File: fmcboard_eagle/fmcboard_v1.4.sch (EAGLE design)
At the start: 138 parts, among them IC1 OPA699ID, IC10 LTC6229IMS8E#TRPBF, IC11 7805TV, IC12 SN74AUC2G66DCTR, IC13 SN74AUC2G66DCTR, IC14 SN74AUC2G66DCTR, IC15 SN74AUC2G66DCTR, IC16 DAC7578SPWR, IC2 DAC7578SPWR, IC3 LTC6229IMS8E#TRPBF, IC4 LTC6229IMS8E#TRPBF, IC5 LM358, IC6 OPA699ID, IC7 OPA699ID, IC8 LTC6229IMS8E#TRPBF, IC9 LTC6229IMS8E#TRPBF, J1 8pin, J10 8pin, J12 4p-2.54, J2 ASP-134604-01, J3 4p-2.54, J4 4p-2.54, J5 8pin, J6 4p-2.54, J7 4p-2.54, J8 4p-2.54, J9 8pin, U1 TXS0108EPWR, U2 STMICROELECTRONICS_L7905ACVST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

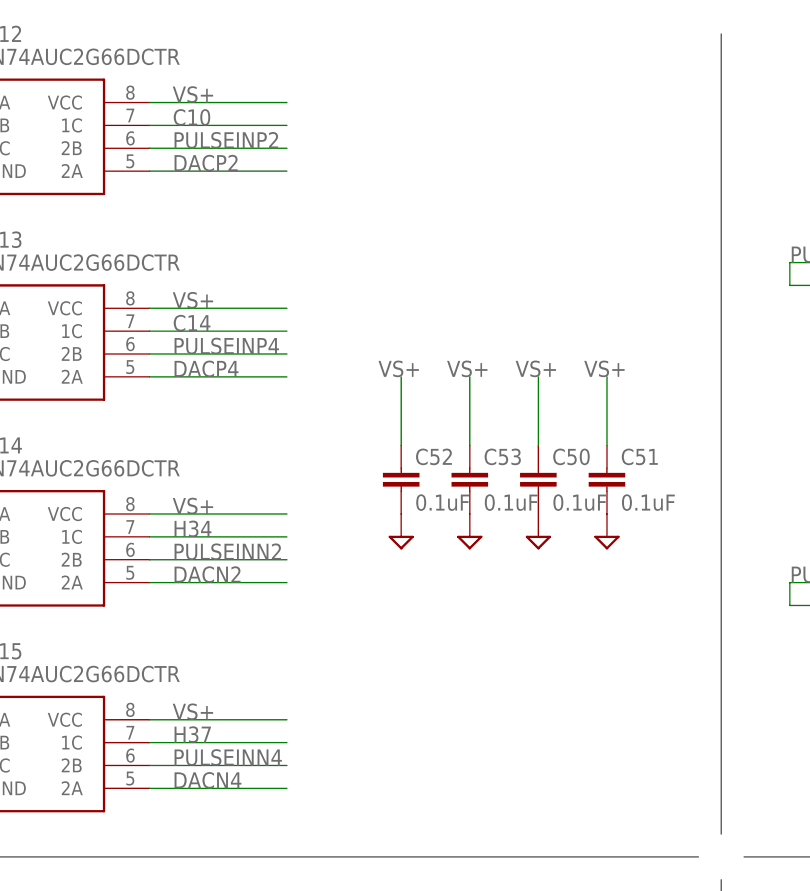
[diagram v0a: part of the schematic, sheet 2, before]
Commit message: v1.41 fix VS+ -> 1V8 for switches
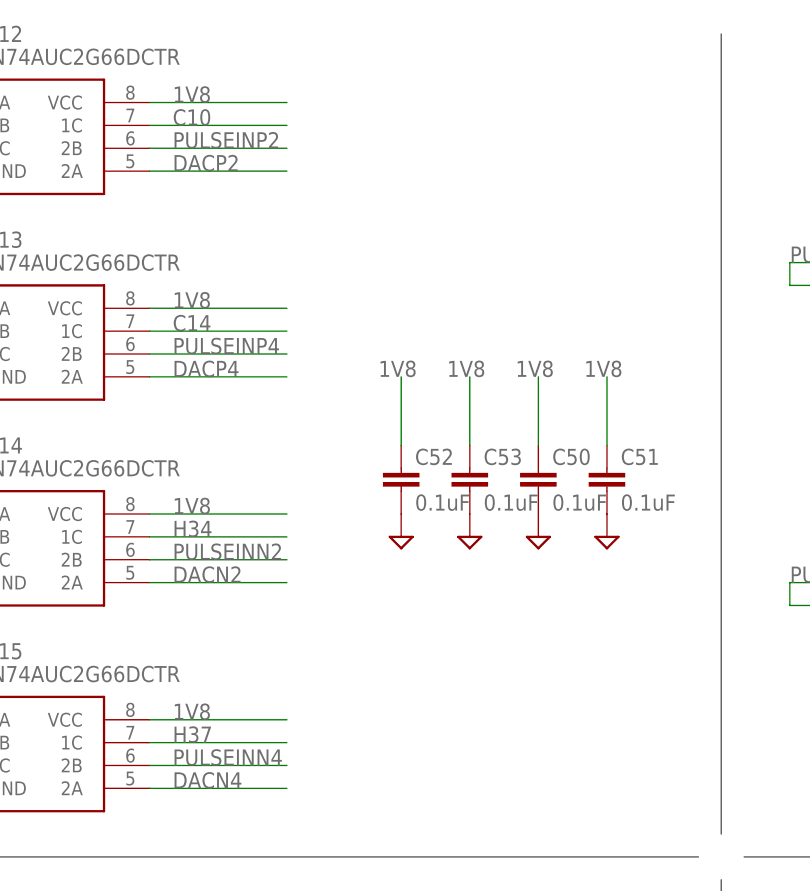
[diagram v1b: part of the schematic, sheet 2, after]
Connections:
- net 1V8: now also C50.1, C51.1, C52.1, C53.1, IC12.VCC, IC13.VCC, IC14.VCC, IC15.VCC
- net VS+: no longer C50.1, C51.1, C52.1, C53.1, IC12.VCC, IC13.VCC, IC14.VCC, IC15.VCC
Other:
- note added: "Pulse and offset DACs"
- note removed: "Pulse DACs"
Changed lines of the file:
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@@
 <text x="132.08" y="114.3" size="1.778" layer="90">Positive output buffers</text>
 <wire x1="190.5" y1="30.48" x2="190.5" y2="119.38" width="0.1524" layer="97"/>
-<text x="81.28" y="114.3" size="1.778" layer="90">Pulse switches</text>
+<text x="86.36" y="114.3" size="1.778" layer="90">Pulse switches</text>
 <wire x1="116.84" y1="27.94" x2="15.24" y2="27.94" width="0.1524" layer="97"/>
 <wire x1="119.38" y1="-15.24" x2="119.38" y2="25.4" width="0.1524" layer="97"/>
 <text x="17.78" y="22.86" size="1.778" layer="90">Pulse resistors for summing</text>
 <wire x1="309.88" y1="27.94" x2="121.92" y2="27.94" width="0.1524" layer="97"/>
-<text x="132.08" y="20.32" size="1.778" layer="90">Pulse DACs</text>
+<text x="132.08" y="20.32" size="1.778" layer="90">Pulse and offset DACs</text>
 </plain>
 <instances>
@@
 <wire x1="259.08" y1="0" x2="259.08" y2="7.62" width="0.1524" layer="91"/>
 <label x="259.08" y="7.62" size="1.778" layer="95"/>
-</segment>
-<segment>
-<pinref part="C52" gate="G$1" pin="1"/>
-<wire x1="83.82" y1="73.66" x2="83.82" y2="81.28" width="0.1524" layer="91"/>
-<label x="81.28" y="81.28" size="1.778" layer="95"/>
-</segment>
-<segment>
-<pinref part="C53" gate="G$1" pin="1"/>
-<wire x1="91.44" y1="73.66" x2="91.44" y2="81.28" width="0.1524" layer="91"/>
-<label x="88.9" y="81.28" size="1.778" layer="95"/>
-</segment>
-<segment>
-<pinref part="C50" gate="G$1" pin="1"/>
-<wire x1="99.06" y1="73.66" x2="99.06" y2="81.28" width="0.1524" layer="91"/>
-<label x="96.52" y="81.28" size="1.778" layer="95"/>
-</segment>
-<segment>
-<pinref part="C51" gate="G$1" pin="1"/>
-<wire x1="106.68" y1="73.66" x2="106.68" y2="81.28" width="0.1524" layer="91"/>
-<label x="104.14" y="81.28" size="1.778" layer="95"/>
-</segment>
-<segment>
-<pinref part="IC12" gate="G$1" pin="VCC"/>
-<wire x1="55.88" y1="111.76" x2="71.12" y2="111.76" width="0.1524" layer="91"/>
-<label x="58.42" y="111.76" size="1.778" layer="95"/>
-</segment>
-<segment>
-<pinref part="IC13" gate="G$1" pin="VCC"/>
-<wire x1="55.88" y1="88.9" x2="71.12" y2="88.9" width="0.1524" layer="91"/>
-<label x="58.42" y="88.9" size="1.778" layer="95"/>
-</segment>
-<segment>
-<pinref part="IC14" gate="G$1" pin="VCC"/>
-<wire x1="55.88" y1="66.04" x2="71.12" y2="66.04" width="0.1524" layer="91"/>
-<label x="58.42" y="66.04" size="1.778" layer="95"/>
-</segment>
-<segment>
-<pinref part="IC15" gate="G$1" pin="VCC"/>
-<wire x1="55.88" y1="43.18" x2="71.12" y2="43.18" width="0.1524" layer="91"/>
-<label x="58.42" y="43.18" size="1.778" layer="95"/>
 </segment>
 <segment>
@@
 <label x="266.7" y="-20.32" size="1.778" layer="95"/>
 </segment>
-</net>
+<segment>
+<pinref part="C52" gate="G$1" pin="1"/>
+<wire x1="83.82" y1="73.66" x2="83.82" y2="81.28" width="0.1524" layer="91"/>
+<label x="81.28" y="81.28" size="1.778" layer="95"/>
+</segment>
+<segment>
+<pinref part="C53" gate="G$1" pin="1"/>
+<wire x1="91.44" y1="73.66" x2="91.44" y2="81.28" width="0.1524" layer="91"/>
+<label x="88.9" y="81.28" size="1.778" layer="95"/>
+</segment>
+<segment>
+<pinref part="C50" gate="G$1" pin="1"/>
+<wire x1="99.06" y1="73.66" x2="99.06" y2="81.28" width="0.1524" layer="91"/>
+<label x="96.52" y="81.28" size="1.778" layer="95"/>
+</segment>
+<segment>
+<pinref part="C51" gate="G$1" pin="1"/>
+<wire x1="106.68" y1="73.66" x2="106.68" y2="81.28" width="0.1524" layer="91"/>
+<label x="104.14" y="81.28" size="1.778" layer="95"/>
+</segment>
+<segment>
+<pinref part="IC12" gate="G$1" pin="VCC"/>
+<wire x1="55.88" y1="111.76" x2="71.12" y2="111.76" width="0.1524" layer="91"/>
+<label x="58.42" y="111.76" size="1.778" layer="95"/>
+</segment>
+<segment>
+<pinref part="IC13" gate="G$1" pin="VCC"/>
+<wire x1="55.88" y1="88.9" x2="71.12" y2="88.9" width="0.1524" layer="91"/>
+<label x="58.42" y="88.9" size="1.778" layer="95"/>
+</segment>
+<segment>
+<pinref part="IC14" gate="G$1" pin="VCC"/>
+<wire x1="55.88" y1="66.04" x2="71.12" y2="66.04" width="0.1524" layer="91"/>
+<label x="58.42" y="66.04" size="1.778" layer="95"/>
+</segment>
+<segment>
+<pinref part="IC15" gate="G$1" pin="VCC"/>
+<wire x1="55.88" y1="43.18" x2="71.12" y2="43.18" width="0.1524" layer="91"/>
+<label x="58.42" y="43.18" size="1.778" layer="95"/>
+</segment>
+</net>

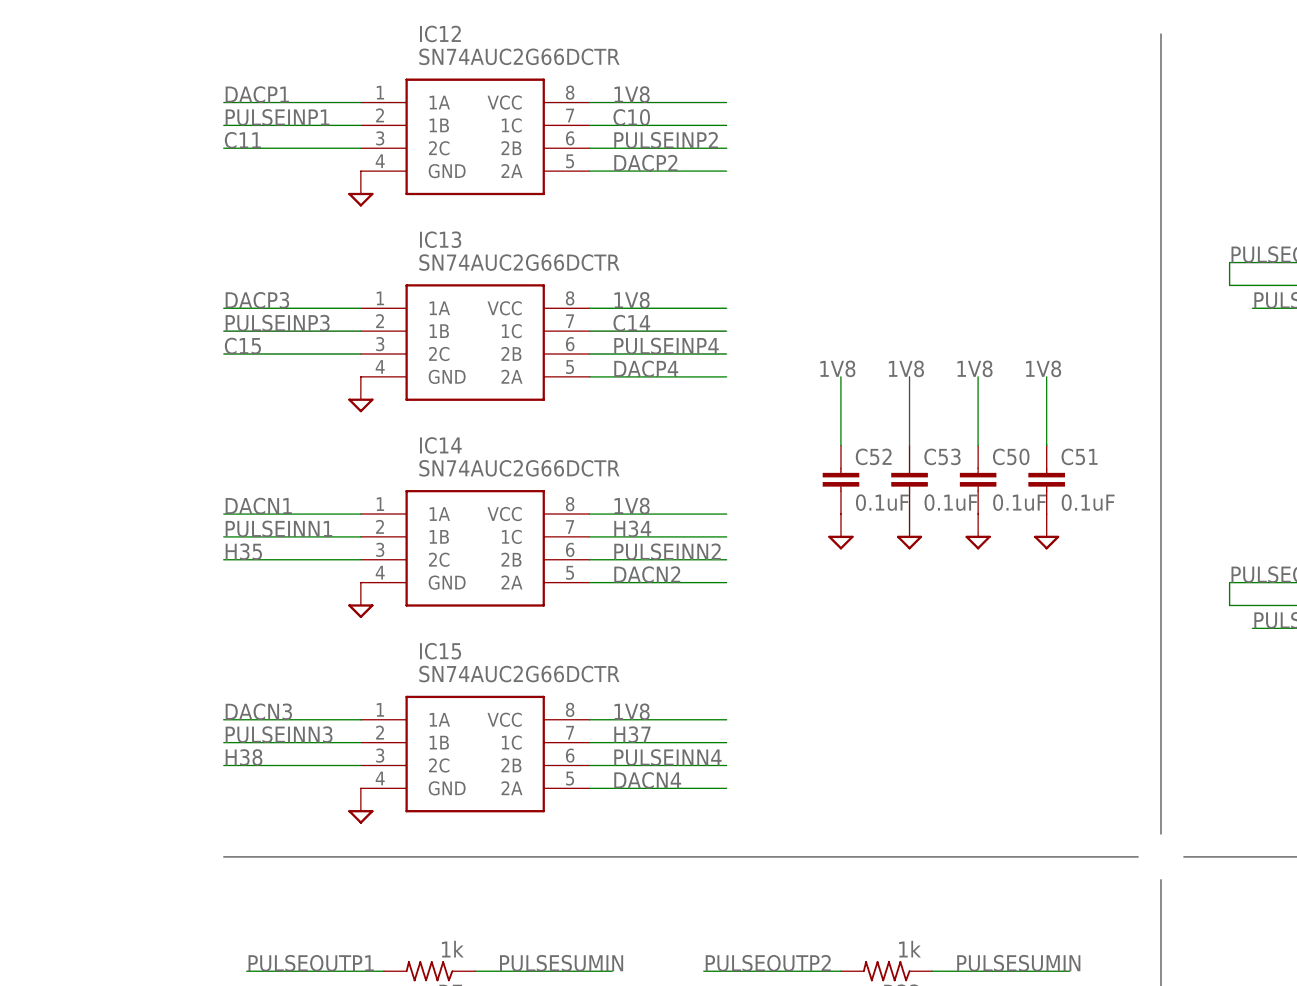
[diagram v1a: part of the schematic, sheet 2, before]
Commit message: v1.42 add 100 Ohm resistors to GND for when switches are off (V should go to GND fast!)
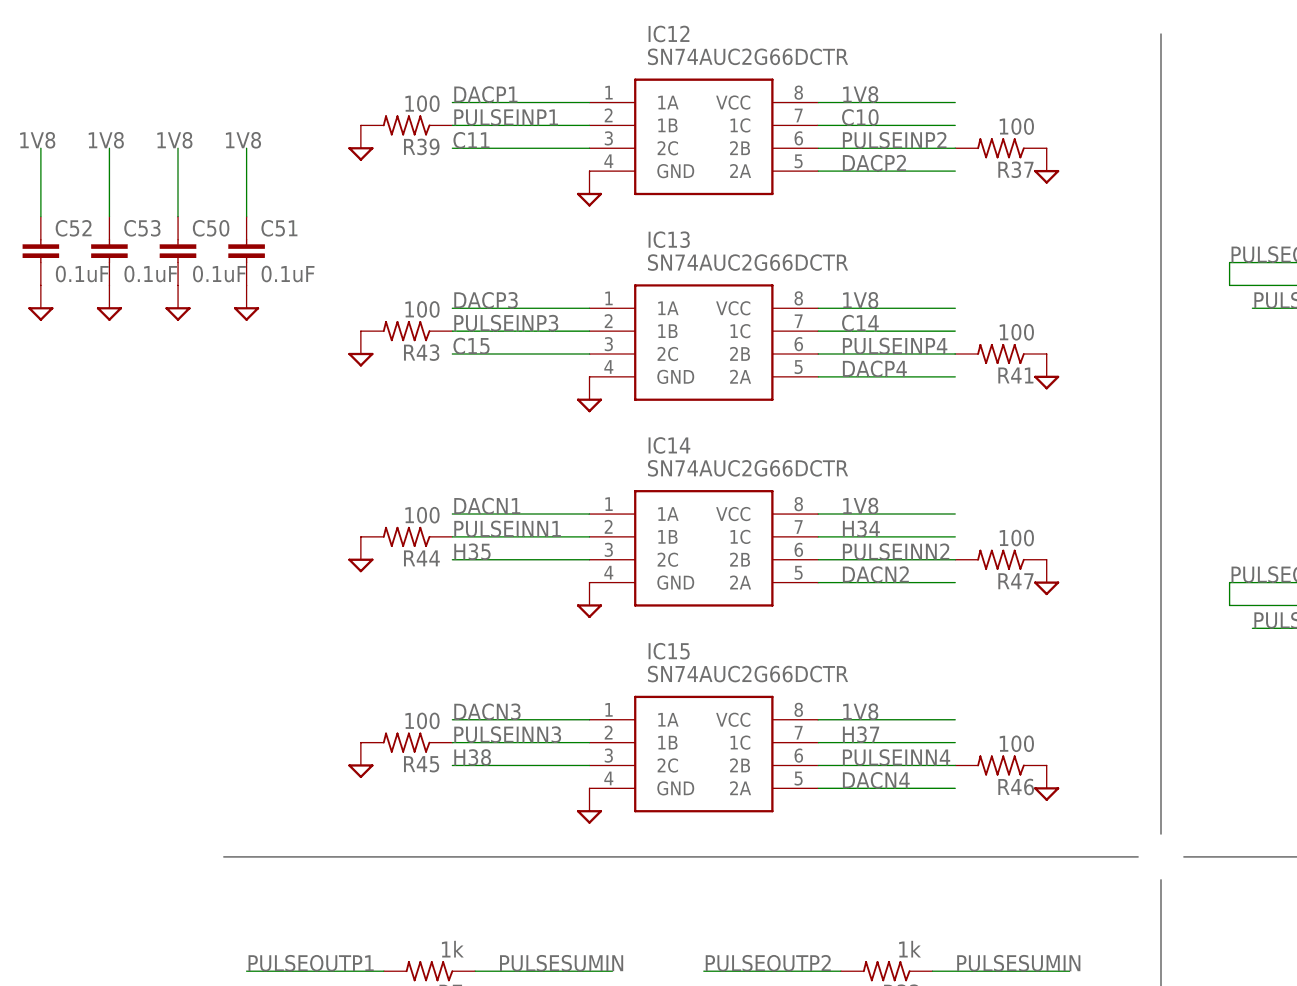
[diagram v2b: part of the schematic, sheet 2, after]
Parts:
- added R37, R39, R41, R43, R44, R45, R46, R47: 100, rcl:R-US_R0805
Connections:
- net GND: now also R37.1, R39.2, R41.1, R43.2, R44.2, R45.2, R46.1, R47.1
- net PULSEINN1: now also R44.1
- net PULSEINN2: now also R47.2
- net PULSEINN3: now also R45.1
- net PULSEINN4: now also R46.2
- net PULSEINP1: now also R39.1
- net PULSEINP2: now also R37.2
- net PULSEINP3: now also R43.1
- net PULSEINP4: now also R41.2
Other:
- moved on the sheet: C50, C51, C52, C53, IC12, IC13, IC14, IC15
